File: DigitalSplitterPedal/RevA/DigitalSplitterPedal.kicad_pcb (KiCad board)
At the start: 2 copper layers, 112.5 x 86.4 mm, 101 parts, among them J1 MonoJack2Switch, J2 Barrel_Jack, J3 MonoJack2Switch, J4 MonoJack2Switch, J5 MonoJack2Switch, J6 MonoJack2Switch, U1 AP7370-50SA-7, U11 TL072, U12 TL074, U14 ISA0505, U15 MCP1754S-3302xCB, U16 TC593002ECB, U2 TL072, U3 TL074, U5 TL072, U6 TL074, U8 TL072, U9 TL074

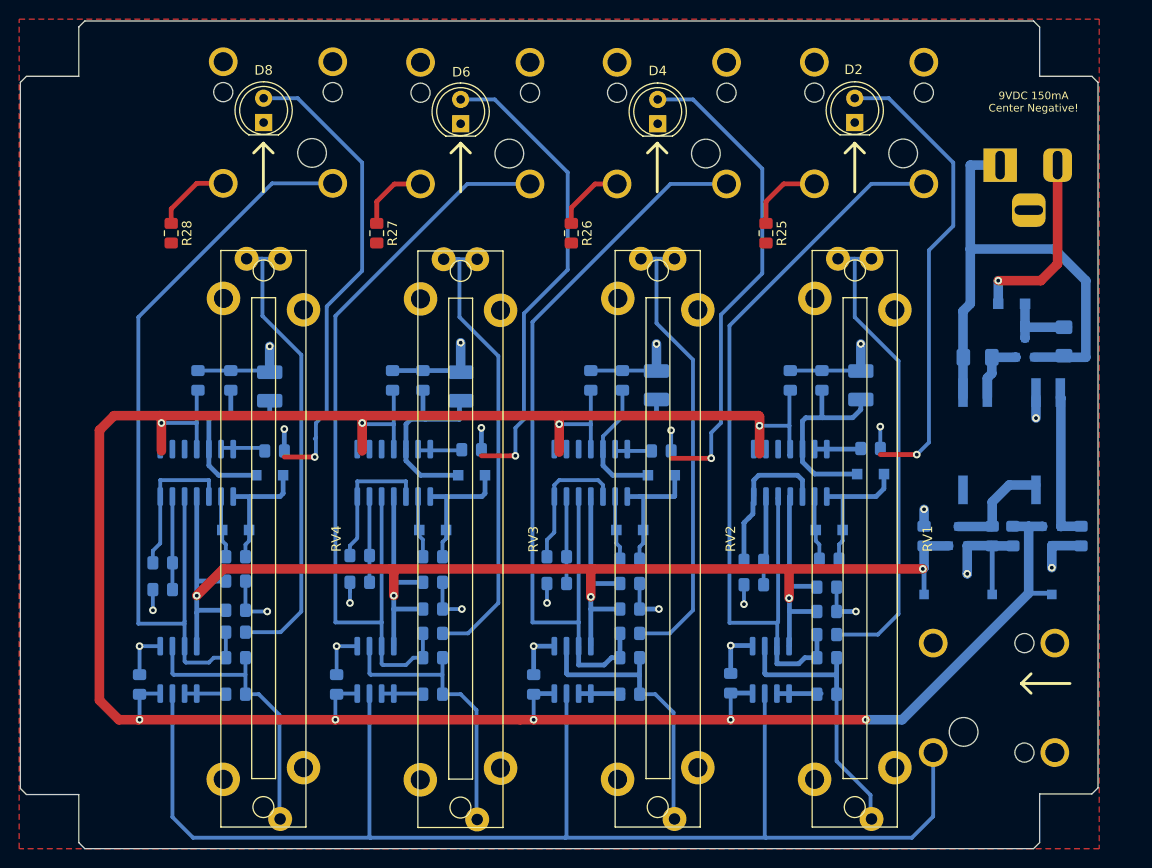
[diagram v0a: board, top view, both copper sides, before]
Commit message: HW update
- Completed RevA layout (draft)
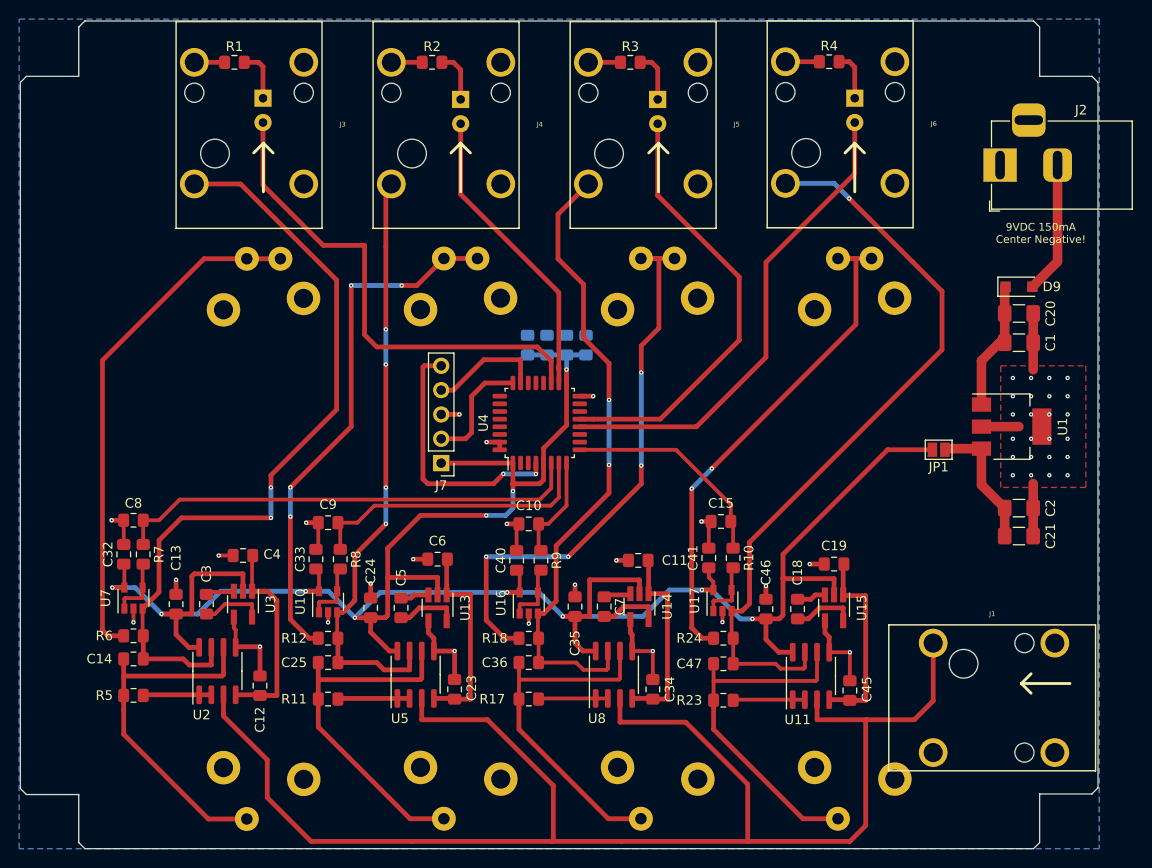
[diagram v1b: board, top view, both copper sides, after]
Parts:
- removed C16, C26, C27, C37, C38: 100nF, Capacitor_SMD:C_0805_2012Metric_Pad1.15x1.40mm_HandSolder
- removed C17, C28, C39: 100nF 1%, Capacitor_SMD:C_1210_3225Metric_Pad1.42x2.65mm_HandSolder
- removed C48, C49, C50: 1uF, Capacitor_SMD:C_0805_2012Metric_Pad1.15x1.40mm_HandSolder
- removed D11, D12, D13, D3, D5, D7: 1N914, Diode_SMD:D_SOD-123F
- removed D4, D6, D8: LED, LED_THT:LED_D5.0mm
- removed R13, R19: 1K, Resistor_SMD:R_0805_2012Metric_Pad1.15x1.40mm_HandSolder
- removed R14, R20: 10K, Resistor_SMD:R_0805_2012Metric_Pad1.15x1.40mm_HandSolder
- removed R15, R21: 220R, Resistor_SMD:R_0805_2012Metric_Pad1.15x1.40mm_HandSolder
- removed R16, R22: 10M 1%, Resistor_SMD:R_0805_2012Metric_Pad1.15x1.40mm_HandSolder
- removed R25, R26, R27, R28: 100R, Capacitor_SMD:C_0805_2012Metric_Pad1.15x1.40mm_HandSolder
- removed TP1, TP2, TP3: TestPoint, TestPoint:TestPoint_Pad_1.0x1.0mm
- removed U12, U6, U9: TL074, Package_SO:SOIC-14_3.9x8.7mm_P1.27mm
- added C11: 1uF, Capacitor_SMD:C_0805_2012Metric_Pad1.15x1.40mm_HandSolder, F.Cu at (144.4, 101.0)
- added C18: 1uF, Capacitor_SMD:C_0805_2012Metric_Pad1.15x1.40mm_HandSolder, F.Cu at (161.0, 106.0)
- added C19: 1uF, Capacitor_SMD:C_0805_2012Metric_Pad1.15x1.40mm_HandSolder, F.Cu at (164.8, 101.3)
- added C20: 1uF, Capacitor_SMD:C_1206_3216Metric_Pad1.42x1.75mm_HandSolder, F.Cu at (184.2, 75.2)
- added C21: 100nF, Capacitor_SMD:C_1206_3216Metric_Pad1.42x1.75mm_HandSolder, F.Cu at (184.2, 98.4)
- added C22: 1uF, Capacitor_SMD:C_0805_2012Metric_Pad1.15x1.40mm_HandSolder, B.Cu at (132.8, 78.5)
- added C29: 100nF, Capacitor_SMD:C_0805_2012Metric_Pad1.15x1.40mm_HandSolder, B.Cu at (134.9, 78.5)
- added C30: 100nF, Capacitor_SMD:C_0805_2012Metric_Pad1.15x1.40mm_HandSolder, B.Cu at (138.9, 78.5)
- added C31: 100nF, Capacitor_SMD:C_0805_2012Metric_Pad1.15x1.40mm_HandSolder, B.Cu at (136.9, 78.5)
- added C32: 100nF, Capacitor_SMD:C_0805_2012Metric_Pad1.15x1.40mm_HandSolder, F.Cu at (90.7, 100.3)
- added C33: 100nF, Capacitor_SMD:C_0805_2012Metric_Pad1.15x1.40mm_HandSolder, F.Cu at (110.7, 100.8)
- added C40: 100nF, Capacitor_SMD:C_0805_2012Metric_Pad1.15x1.40mm_HandSolder, F.Cu at (131.7, 101.0)
- added C41: 100nF, Capacitor_SMD:C_0805_2012Metric_Pad1.15x1.40mm_HandSolder, F.Cu at (151.8, 100.7)
- added D14: LED, LED_THT:LED_D5.0mm, B.Cu at (167.0, 52.7)
- added J7: Conn_01x05, Connector_PinHeader_2.54mm:PinHeader_1x05_P2.54mm_Vertical, F.Cu at (123.8, 90.8)
- added JP1: Jumper_NO_Small, Jumper:SolderJumper-2_P1.3mm_Open_Pad1.0x1.5mm, F.Cu at (175.8, 89.4)
- added U10: MCP601-xOT, Package_TO_SOT_SMD:SOT-23-5, F.Cu at (112.0, 105.3)
- added U13: TPS60400, Package_TO_SOT_SMD:SOT-23-5_HandSoldering, F.Cu at (123.4, 105.9)
- added U17: MCP601-xOT, Package_TO_SOT_SMD:SOT-23-5, F.Cu at (153.2, 105.2)
- added U4: STM32F051K8Tx, Package_QFP:LQFP-32_7x7mm_P0.8mm, F.Cu at (134.1, 86.6)
- added U7: MCP601-xOT, Package_TO_SOT_SMD:SOT-23-5, F.Cu at (91.7, 104.9)
- C1, C12, C13, C14, C15, C2, C23, C24, C25, C3, C34, C35, C36, C45, C46, C47, D9, J1, J2, J3, J4, J5, J6, R11, R12, R17, R18, R23, R24, R5, R6, U11, U2, U5, U8: moved to F.Cu
- C10, C8, C9: value 1nF -> 100nF; moved to F.Cu
- C4, C5: value 100nF -> 1uF; moved to F.Cu
- C6: value 100nF 1% -> 1uF; footprint Capacitor_SMD:C_1210_3225Metric_Pad1.42x2.65mm_HandSolder -> Capacitor_SMD:C_0805_2012Metric_Pad1.15x1.40mm_HandSolder; moved to F.Cu
- C7: value 1nF -> 1uF; moved to F.Cu
- D1, D10: value 1N914 -> LED; footprint Diode_SMD:D_SOD-123F -> LED_THT:LED_D5.0mm
- D2, RV1, RV2, RV3, RV4: moved to B.Cu
- R1: value 1K -> R; moved to F.Cu
- R10: value 10M 1% -> 50R; moved to F.Cu
- R2: value 10K -> R; moved to F.Cu
- R3: value 220R -> R; moved to F.Cu
- R4: value 10M 1% -> R; moved to F.Cu
- R7: value 1K -> 50R; moved to F.Cu
- R8: value 10K -> 50R; moved to F.Cu
- R9: value 220R -> 50R; moved to F.Cu
- U1: value AP7370-50SA-7 -> MCP1703A-3302_SOT223; footprint Package_TO_SOT_SMD:SOT-23 -> Package_TO_SOT_SMD:SOT-223-3_TabPin2; moved to F.Cu
- U14: value ISA0505 -> TPS60400; footprint XP_ISA:ISA0505 -> Package_TO_SOT_SMD:SOT-23-5_HandSoldering; moved to F.Cu
- U15: value MCP1754S-3302xCB -> TPS60400; footprint Package_TO_SOT_SMD:SOT-23 -> Package_TO_SOT_SMD:SOT-23-5_HandSoldering; moved to F.Cu
- U16: value TC593002ECB -> MCP601-xOT; footprint Package_TO_SOT_SMD:SOT-23 -> Package_TO_SOT_SMD:SOT-23-5; moved to F.Cu
- U3: value TL074 -> TPS60400; footprint Package_SO:SOIC-14_3.9x8.7mm_P1.27mm -> Package_TO_SOT_SMD:SOT-23-5_HandSoldering; moved to F.Cu
- moved C3 82.3 mm to (99.3, 105.5)
- moved R1 76.9 mm to (102.2, 49.0)
- moved D1 74.6 mm to (105.2, 52.7), turned to 270 degrees
- moved C45 74.2 mm to (166.5, 114.6)
- moved C14 72.4 mm to (91.7, 111.3), turned to 180 degrees
- moved R5 72.4 mm to (91.7, 115.1), turned to 0 degrees
- moved R6 72.4 mm to (91.7, 108.8), turned to 180 degrees
- moved C13 67.9 mm to (96.1, 105.5), turned to 90 degrees
- moved U11 66.0 mm to (162.4, 113.0)
- moved J3 64.7 mm to (103.8, 55.5)
- moved R2 61.9 mm to (122.9, 49.0), turned to 0 degrees
- moved RV4 61.7 mm to (167.0, 98.7)
- moved RV1 61.7 mm to (105.3, 98.7)
- moved C4 61.0 mm to (103.1, 100.5), turned to 180 degrees
- moved U3 58.8 mm to (103.1, 105.5), turned to 270 degrees
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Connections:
- net /InputBuffer1/SIGNAL_INPUT renamed /InputBufferAndGain1/SIGNAL_INPUT
- net /sheet5F6A30A3/SIGNAL_INPUT renamed /PEAK_IN_BUF2
- net /sheet5F6AEF15/SIGNAL_INPUT renamed /PEAK_IN_BUF4
- C1 pad 1: /PowerSupply/+9V_POL -> Net-(C1-Pad1)
- C10 pad 1: Net-(C10-Pad1) -> /PeakDetectorMCU/PEAK_IN_ADC3
- C10 pad 2: Net-(C10-Pad2) -> GNDS
- C12 pad 1: -3V3 -> /InputBufferAndGain1/NEGVIN
- C12 pad 2: VCOM -> GNDS
- C13 pad 2: VCOM -> GNDS
- C14 pad 1: /PeakDetector1/SIGNAL_INPUT -> /PEAK_IN_BUF1
- C15 pad 1: +3V3 -> /PeakDetectorMCU/PEAK_IN_ADC4
- C15 pad 2: VCOM -> GNDS
- C2 pad 1: /PowerSupply/+5V_REG -> Net-(C2-Pad1)
- C23 pad 1: -3V3 -> /InputBufferAndGain2/NEGVIN
- C23 pad 2: VCOM -> GNDS
- C24 pad 2: VCOM -> GNDS
- C3 pad 2: VCOM -> Net-(C3-Pad2)
- C34 pad 1: -3V3 -> /InputBufferAndGain3/NEGVIN
- C34 pad 2: VCOM -> GNDS
- C35 pad 2: VCOM -> GNDS
- C36 pad 1: /sheet5F6A444D/SIGNAL_INPUT -> /PEAK_IN_BUF3
- C4 pad 1: +3V3 -> /InputBufferAndGain1/NEGVIN
- C4 pad 2: VCOM -> GNDS
- C45 pad 1: -3V3 -> /InputBufferAndGain4/NEGVIN
- C45 pad 2: VCOM -> GNDS
- C46 pad 2: VCOM -> GNDS
- C5 pad 1: -3V3 -> Net-(C5-Pad1)
- C5 pad 2: VCOM -> Net-(C5-Pad2)
- C6 pad 1: Net-(C6-Pad1) -> /InputBufferAndGain2/NEGVIN
- C6 pad 2: VCOM -> GNDS
- C8 pad 1: Net-(C8-Pad1) -> /PeakDetectorMCU/PEAK_IN_ADC1
- C8 pad 2: Net-(C8-Pad2) -> GNDS
- C9 pad 1: Net-(C9-Pad1) -> /PeakDetectorMCU/PEAK_IN_ADC2
- C9 pad 2: Net-(C9-Pad2) -> GNDS
- D1 pad 1: Net-(C6-Pad1) -> Net-(D1-Pad1)
- D1 pad 2: Net-(C7-Pad1) -> /PeakDetectorMCU/PEAK_OUT_PWM4
- D10 pad 1: Net-(C7-Pad1) -> Net-(D10-Pad1)
- D10 pad 2: Net-(C7-Pad2) -> /PeakDetectorMCU/PEAK_OUT_PWM2
- D2 pad 1: VCOM -> Net-(D2-Pad1)
- D2 pad 2: Net-(D2-Pad2) -> /PeakDetectorMCU/PEAK_OUT_PWM3
- D9 pad 1: /PowerSupply/+9V_POL -> Net-(C1-Pad1)
- J1 pad 2: VCOM -> GNDS
- J1 pad 3: VCOM -> GNDS
- J1 pad 4: VCOM -> GNDS
- J3 pad 1: /PeakDetector1/SIGNAL_INPUT -> /PEAK_IN_BUF1
- J3 pad 3: VCOM -> GNDS
- J3 pad 4: VCOM -> GNDS
- J4 pad 3: VCOM -> GNDS
- J4 pad 4: VCOM -> GNDS
- J5 pad 1: /sheet5F6A444D/SIGNAL_INPUT -> /PEAK_IN_BUF3
- J5 pad 3: VCOM -> GNDS
- J5 pad 4: VCOM -> GNDS
- J6 pad 3: VCOM -> GNDS
- J6 pad 4: VCOM -> GNDS
- R1 pad 1: VCOM -> GNDS
- R1 pad 2: Net-(R1-Pad2) -> Net-(D1-Pad1)
- R10 pad 1: VCOM -> /PeakDetectorMCU/PEAK_IN_ADC4
- R18 pad 1: /sheet5F6A444D/SIGNAL_INPUT -> /PEAK_IN_BUF3
- R2 pad 1: Net-(R1-Pad2) -> GNDS
- R2 pad 2: Net-(R2-Pad2) -> Net-(D2-Pad1)
- R3 pad 1: Net-(D2-Pad2) -> GNDS
- R3 pad 2: Net-(R3-Pad2) -> Net-(D10-Pad1)
- R4 pad 1: VCOM -> GNDS
- R4 pad 2: Net-(C6-Pad1) -> Net-(D14-Pad1)
- R6 pad 1: /PeakDetector1/SIGNAL_INPUT -> /PEAK_IN_BUF1
- R7 pad 1: VCOM -> /PeakDetectorMCU/PEAK_IN_ADC1
- R8 pad 1: Net-(R7-Pad2) -> /PeakDetectorMCU/PEAK_IN_ADC2
- R9 pad 1: Net-(D4-Pad2) -> /PeakDetectorMCU/PEAK_IN_ADC3
- U1 pad 1: GNDS -> Net-(C1-Pad1)
- U1 pad 2: /PowerSupply/+5V_REG -> GNDS
- U1 pad 3: /PowerSupply/+9V_POL -> Net-(C2-Pad1)
- U11 pad 4: -3V3 -> /InputBufferAndGain4/NEGVIN
- U11 pad 5: VCOM -> GNDS
- U14 pad 1: GNDS -> /InputBufferAndGain3/NEGVIN
- U14 pad 2: /PowerSupply/+5V_REG -> +3V3
- U14 pad 4: VCOM -> GNDS
- U14 pad 5: Net-(C48-Pad2) -> Net-(C7-Pad2)
- U15 pad 1: VCOM -> /InputBufferAndGain4/NEGVIN
- U15 pad 3: Net-(C3-Pad1) -> Net-(C18-Pad1)
- U16 pad 1: -3V3 -> Net-(R9-Pad2)
- U16 pad 2: Net-(C48-Pad2) -> GNDS
- U16 pad 3: VCOM -> /PEAK_IN_BUF3
- U2 pad 4: -3V3 -> /InputBufferAndGain1/NEGVIN
- U2 pad 5: VCOM -> GNDS
- U2 pad 7: /PeakDetector1/SIGNAL_INPUT -> /PEAK_IN_BUF1
- U3 pad 1: Net-(C7-Pad1) -> /InputBufferAndGain1/NEGVIN
- U3 pad 2: Net-(C7-Pad2) -> +3V3
- U3 pad 3: Net-(R2-Pad2) -> Net-(C3-Pad1)
- U3 pad 4: +3V3 -> GNDS
- U3 pad 5: /PeakDetector1/SIGNAL_INPUT -> Net-(C3-Pad2)
- U5 pad 4: -3V3 -> /InputBufferAndGain2/NEGVIN
- U5 pad 5: VCOM -> GNDS
- U8 pad 4: -3V3 -> /InputBufferAndGain3/NEGVIN
- U8 pad 5: VCOM -> GNDS
- U8 pad 7: /sheet5F6A444D/SIGNAL_INPUT -> /PEAK_IN_BUF3
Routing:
- net -3V3: track 288.8 -> 0.00 mm, vias 9 -> 0
- net VCOM: track 110.1 -> 0.00 mm, vias 20 -> 0
- net /sheet5F6A444D/SIGNAL_INPUT: track 87.9 -> 0.00 mm
- net /PeakDetector1/SIGNAL_INPUT: track 86.7 -> 0.00 mm
- net /PEAK_IN_BUF1: track 0.00 -> 81.8 mm, vias 0 -> 2
- net /PEAK_IN_BUF3: track 0.00 -> 66.5 mm, vias 0 -> 2
- net +3V3: track 180.6 -> 243.4 mm, vias 5 -> 11
- net Net-(D4-Pad2): track 52.8 -> 0.00 mm, vias 2 -> 0
- net Net-(D6-Pad2): track 52.8 -> 0.00 mm, vias 2 -> 0
- net /PeakDetectorMCU/PEAK_OUT_PWM4: track 0.00 -> 52.0 mm
- net Net-(D8-Pad2): track 51.3 -> 0.00 mm, vias 2 -> 0
- net Net-(D2-Pad2): track 51.2 -> 0.00 mm, vias 2 -> 0
- net /PeakDetectorMCU/PEAK_OUT_PWM1: track 0.00 -> 50.8 mm
- net /PeakDetectorMCU/PEAK_IN_ADC1: track 0.00 -> 49.1 mm
- net GNDS: track 54.6 -> 100.8 mm, vias 0 -> 47
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- added copper zone on B.Cu, net GNDS
- added copper zone on F.Cu, net GNDS
- removed copper zone on F.Cu, net VCOM
